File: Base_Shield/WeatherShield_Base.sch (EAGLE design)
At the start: 78 parts, among them Q1 BSS138, Q2 BSS138, U1 DS3231SN, U2 LT3652, U4 MPL3115A2LGA8, U5 HTU21D

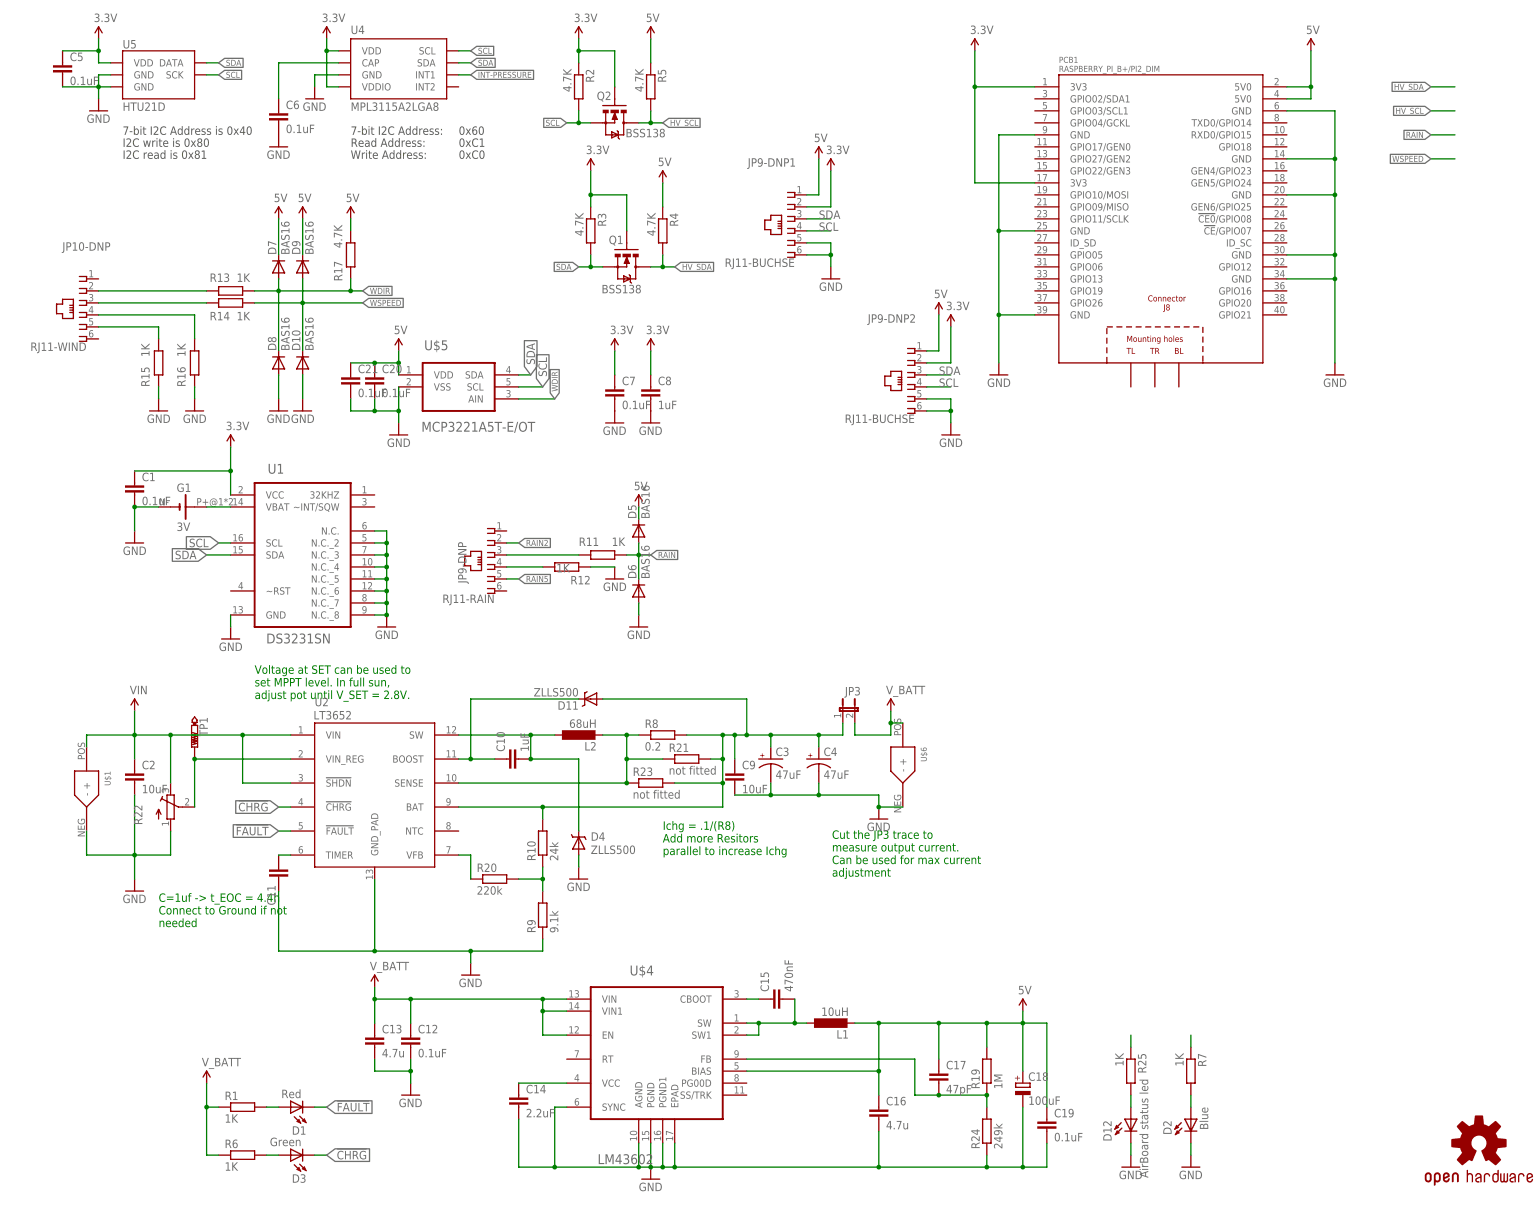
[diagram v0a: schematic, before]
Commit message: WeatherShield v1
Restructuration des Fichiers
Division en Air et Base Board
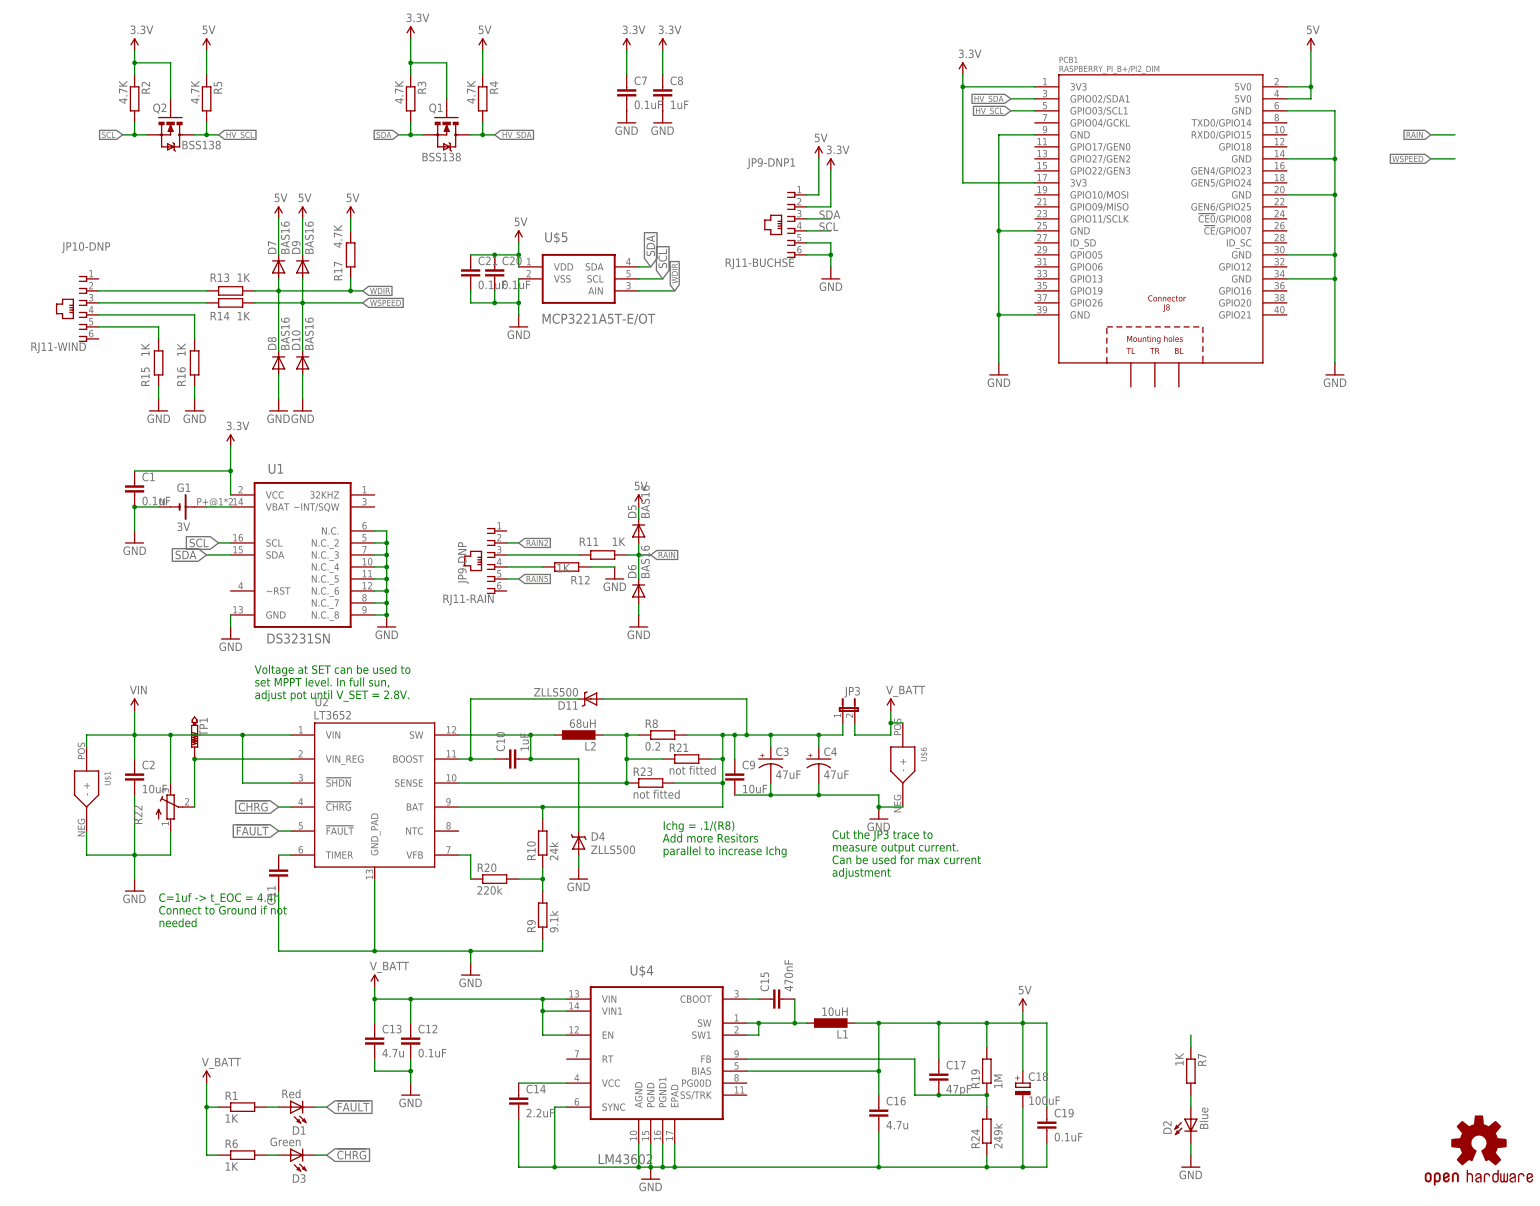
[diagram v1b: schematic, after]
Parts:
- removed C5, C6: 0.1uF, rcl:C-EUC0603
- removed D12: AirBoard status led, SparkFun:LED0603
- removed JP9-DNP2: RJ11-BUCHSE, FSEWeatherShield:RJ11-BUCHSE
- removed R25: 1K, rcl:R-EU_R0603
- removed U4: MPL3115A2LGA8, SparkFun-Sensors:MPL3115A2LGA8
- removed U5: HTU21D, SparkFun-Sensors:HTU21DSMD
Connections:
- removed net INT-PRESSURE: U4.INT1
- removed net N$28: D12.A, R25.2
- removed net N$5: C6.1, U4.CAP
- removed net STAT1: R25.1
- net 3.3V: no longer C5.1, JP9-DNP2.2, U4.VDD, U4.VDDIO, U5.VDD
- net 5V: no longer JP9-DNP2.1
- net GND: no longer C5.2, C6.2, D12.C, JP9-DNP2.5, JP9-DNP2.6, U4.GND, U5.GND@2, U5.GND@7
- net HV_SCL: now also PCB1.GPIO03/SCL1
- net HV_SDA: now also PCB1.GPIO02/SDA1
- net SCL: no longer JP9-DNP2.4, U4.SCL, U5.SCK
- net SDA: no longer JP9-DNP2.3, U4.SDA, U5.DATA
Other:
- note removed: "0x60"
- note removed: "0xC0"
- note removed: "0xC1"
- note removed: "7-bit I2C Address is 0x40"
- note removed: "7-bit I2C Address:"
- note removed: "Humidity"
- note removed: "I2C read is 0x81"
- note removed: "I2C write is 0x80"
- note removed: "Pressure"
- note removed: "Read Address:"
- note removed: "Write Address:"
- moved on the sheet: C20, C21, C7, C8, Q1, Q2, R2, R3, R4, R5, U$5

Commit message: WeatherShield_v1
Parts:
- removed U$5: MCP3221A5T-E/OT, FSEWeatherShield:MCP3221A5T-E/OT
- added C5: 0.1uF, rcl:C-EUC0603
- added JP1, JP2, JP4: (no value), pinhead:PINHD-1X2
- added JP5: (no value), pinhead:PINHD-1X3
- added JP6, JP7, JP8: (no value), pinhead:PINHD-1X1
- added U3: TMP100MDBVREP, FSEWeatherShield:TMP100MDBVREP
- added U4: ADS1015IDGST, FSEWeatherShield:ADS1015IDGST
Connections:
- new net N$14: JP6.1, U4.AIN1
- new net N$18: JP4.1, PCB1.TXD0/GPIO14
- new net N$19: JP4.2, PCB1.RXD0/GPIO15
- new net N$20: JP5.3, PCB1.GPIO10/MOSI
- new net N$21: JP5.2, PCB1.GPIO09/MISO
- new net N$25: JP5.1, PCB1.GPIO11/SCLK
- new net N$8: JP7.1, U4.AIN2
- new net N$9: JP8.1, U4.AIN3
- net 3.3V: now also C5.1, JP2.1, U3.V+
- net 5V: now also JP1.1, U4.VDD; no longer C20.1, C21.1, U$5.VDD
- net GND: now also C5.2, JP1.2, JP2.2, U3.AD0, U3.AD1, U3.GND, U4.ADDR, U4.GND; no longer C20.2, C21.2, U$5.VSS
- net HV_SCL: now also U4.SCL; no longer PCB1.GPIO03/SCL1
- net HV_SDA: now also U4.SDA; no longer PCB1.GPIO02/SDA1
- net RAIN: now also PCB1.GPIO18
- net SCL: now also PCB1.GPIO03/SCL1, U3.SCL; no longer U$5.SCL
- net SDA: now also PCB1.GPIO02/SDA1, U3.SDA; no longer U$5.SDA
- net STAT3: now also PCB1.GPIO21
- net WDIR: now also U4.AIN0; no longer U$5.AIN
- net WSPEED: now also PCB1.GPIO17/GEN0
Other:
- note added: "7-Bit I2C Address is 0x48"
- note added: "7-Bit I2C Address is 0x68"
- note added: "Add. SPI"
- note added: "Add. UART"
- note added: "Air Board Interface"
- note added: "Level shifter"
- note added: "Solar cell"
- note added: "Temperatur sensor"
- moved on the sheet: C1, C10, C11, C12, C13, C14, C15, C16, C17, C18, C19, C2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

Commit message: WeatherShield_v1
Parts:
- removed D10, D5, D6, D7, D8, D9: BAS16, SparkFun:DIODESOD
- removed R11, R13, R15, R16: 1K, rcl:R-EU_R0603
- R12, R14: value 1K -> 3k9
- R17: value 4.7K -> 10k
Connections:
- removed net N$1: JP10-DNP.3, R14.2
- removed net N$11: JP9-DNP.4, R12.1
- removed net N$12: JP10-DNP.5, R15.1
- removed net N$13: JP10-DNP.4, R16.1
- removed net N$2: JP10-DNP.2, R13.2
- removed net N$4: JP9-DNP.3, R11.2
- removed net RAIN2: JP9-DNP.2
- removed net RAIN5: JP9-DNP.5
- net 3.3V: now also JP10-DNP.3, JP9-DNP.3
- net 5V: no longer D5.C, D7.C, D9.C
- net GND: now also JP10-DNP.5, R14.2; no longer D10.A, D6.A, D8.A, R15.2, R16.2
- net RAIN: now also JP9-DNP.4, R12.1; no longer D5.A, D6.C, R11.1
- net WDIR: now also JP10-DNP.2; no longer D7.A, D8.C, R13.1
- net WSPEED: now also JP10-DNP.4; no longer D10.C, D9.A
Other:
- note added: "ADC 2 I2C"
- moved on the sheet: JP6, JP7, JP8, JP9-DNP, R12, R14, R17, U4

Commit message: WeatherShield_v1
routing....
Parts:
- added C6: 0.1uF, rcl:C-EUC0603
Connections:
- net 5V: now also C6.1
- net GND: now also C6.2
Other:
- moved on the sheet: C21
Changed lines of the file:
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@@
 <part name="P+6" library="SparkFun" deviceset="3.3V" device=""/>
 <part name="P+8" library="SparkFun" deviceset="3.3V" device=""/>
+<part name="C6" library="rcl" deviceset="C-EU" device="C0603" value="0.1uF"/>
 </parts>
 <sheets>
@@
 <instance part="GND23" gate="1" x="363.22" y="111.76" rot="MR0"/>
 <instance part="C20" gate="G$1" x="213.36" y="203.2"/>
-<instance part="C21" gate="G$1" x="208.28" y="203.2"/>
+<instance part="C21" gate="G$1" x="223.52" y="205.74"/>
 <instance part="R22" gate="1" x="40.64" y="48.26"/>
 <instance part="JP9-DNP1" gate="G$1" x="165.1" y="238.76" smashed="yes" rot="MR0">
@@
 <instance part="C5" gate="G$1" x="147.32" y="121.92"/>
 <instance part="GND18" gate="1" x="91.44" y="162.56" rot="MR0"/>
-<instance part="SUPPLY14" gate="G$1" x="73.66" y="203.2"/>
+<instance part="SUPPLY14" gate="G$1" x="73.66" y="210.82"/>
 <instance part="U4" gate="A" x="96.52" y="185.42"/>
 <instance part="JP6" gate="G$1" x="68.58" y="175.26" rot="R180"/>
@@
 <instance part="GND3" gate="1" x="172.72" y="172.72" rot="MR0"/>
 <instance part="P+6" gate="G$1" x="172.72" y="203.2"/>
-<instance part="P+8" gate="G$1" x="22.86" y="187.96"/>
+<instance part="P+8" gate="G$1" x="22.86" y="203.2"/>
+<instance part="C6" gate="G$1" x="66.04" y="203.2"/>
 </instances>
 <busses>
@@
 <pinref part="U4" gate="A" pin="ADDR"/>
 <wire x1="91.44" y1="167.64" x2="91.44" y2="170.18" width="0.1524" layer="91"/>
-<wire x1="76.2" y1="190.5" x2="60.96" y2="190.5" width="0.1524" layer="91"/>
+<wire x1="76.2" y1="190.5" x2="66.04" y2="190.5" width="0.1524" layer="91"/>
+<wire x1="66.04" y1="190.5" x2="60.96" y2="190.5" width="0.1524" layer="91"/>
 <wire x1="60.96" y1="190.5" x2="60.96" y2="167.64" width="0.1524" layer="91"/>
 <wire x1="60.96" y1="167.64" x2="91.44" y2="167.64" width="0.1524" layer="91"/>
 <junction x="91.44" y="167.64"/>
+<pinref part="C6" gate="G$1" pin="2"/>
+<wire x1="66.04" y1="198.12" x2="66.04" y2="190.5" width="0.1524" layer="91"/>
+<junction x="66.04" y="190.5"/>
 </segment>
 <segment>
@@
 <pinref part="P+8" gate="G$1" pin="3.3V"/>
 <wire x1="15.24" y1="182.88" x2="22.86" y2="182.88" width="0.1524" layer="91"/>
-<wire x1="22.86" y1="182.88" x2="22.86" y2="187.96" width="0.1524" layer="91"/>
+<wire x1="22.86" y1="182.88" x2="22.86" y2="203.2" width="0.1524" layer="91"/>
 </segment>
 </net>
@@
 <segment>
 <wire x1="76.2" y1="195.58" x2="73.66" y2="195.58" width="0.1524" layer="91" style="longdash"/>
-<wire x1="73.66" y1="195.58" x2="73.66" y2="203.2" width="0.1524" layer="91" style="longdash"/>
+<wire x1="73.66" y1="195.58" x2="73.66" y2="208.28" width="0.1524" layer="91"/>
 <pinref part="SUPPLY14" gate="G$1" pin="5V"/>
 <pinref part="U4" gate="A" pin="VDD"/>
-</segment>
-</net>
+<pinref part="C6" gate="G$1" pin="1"/>
+<wire x1="73.66" y1="208.28" x2="73.66" y2="210.82" width="0.1524" layer="91"/>
+<wire x1="66.04" y1="205.74" x2="66.04" y2="208.28" width="0.1524" layer="91"/>
+<wire x1="66.04" y1="208.28" x2="73.66" y2="208.28" width="0.1524" layer="91"/>
+<junction x="73.66" y="208.28"/>
+</segment>
+</net>

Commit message: WeatherShield_v1
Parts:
- removed C20, C21: 0.1uF, rcl:C-EUC0603
- removed LOGO1: OSHW-LOGOM, SparkFun-Aesthetics:OSHW-LOGOM
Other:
- note added: "+5V Generation (Raspberry Power)"
- moved on the sheet: C1, C10, C11, C12, C13, C14, C15, C16, C17, C18, C19, C2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

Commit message: WeatherShield_v1
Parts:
- renumbered U$1 to SOLAR_CELL, U$6 to BATT
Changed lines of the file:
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@@
 <part name="SUPPLY12" library="SparkFun-Aesthetics" deviceset="5V" device=""/>
 <part name="P+1" library="SparkFun" deviceset="VCC" device="" value="3.3V"/>
-<part name="U$1" library="FSEWeatherShield" deviceset="XT-60" device=""/>
-<part name="U$6" library="FSEWeatherShield" deviceset="XT-60" device=""/>
+<part name="SOLAR_CELL" library="FSEWeatherShield" deviceset="XT-60" device=""/>
+<part name="BATT" library="FSEWeatherShield" deviceset="XT-60" device=""/>
 <part name="JP1" library="pinhead" deviceset="PINHD-1X2" device=""/>
 <part name="JP2" library="pinhead" deviceset="PINHD-1X2" device=""/>
@@
 <text x="172.72" y="71.12" size="1.778" layer="95">Add. SPI</text>
 <text x="159.258" y="8.382" size="2.54" layer="98" rot="R90">Level shifter</text>
-<text x="129.794" y="135.636" size="1.27" layer="98" rot="R180">Air Board Interface</text>
+<text x="132.334" y="133.096" size="1.27" layer="98" rot="R180">Air Board Interface</text>
 <text x="68.326" y="174.244" size="1.27" layer="98">Solar cell</text>
 <text x="2.54" y="106.68" size="1.27" layer="98">Temperatur sensor</text>
@@
 <instance part="C12" gate="G$1" x="10.16" y="33.02"/>
 <instance part="C19" gate="G$1" x="111.76" y="15.24"/>
-<instance part="SUPPLY13" gate="G$1" x="254" y="106.68"/>
+<instance part="SUPPLY13" gate="G$1" x="248.92" y="114.3"/>
 <instance part="GND22" gate="1" x="182.88" y="45.72" rot="MR0"/>
 <instance part="GND23" gate="1" x="259.08" y="66.04" rot="MR270"/>
@@
 <instance part="SUPPLY16" gate="G$1" x="134.62" y="134.62"/>
 <instance part="P+5" gate="G$1" x="137.16" y="132.08"/>
-<instance part="P+7" gate="G$1" x="175.26" y="109.22"/>
+<instance part="P+7" gate="G$1" x="175.26" y="114.3"/>
 <instance part="SUPPLY12" gate="G$1" x="104.14" y="38.1"/>
 <instance part="P+1" gate="1" x="129.54" y="99.06"/>
-<instance part="U$1" gate="G$1" x="7.62" y="157.48" rot="R270"/>
-<instance part="U$6" gate="G$1" x="180.34" y="162.56" rot="R270"/>
+<instance part="SOLAR_CELL" gate="G$1" x="7.62" y="157.48" rot="R270"/>
+<instance part="BATT" gate="G$1" x="180.34" y="162.56" rot="R270"/>
 <instance part="JP1" gate="G$1" x="259.08" y="144.78"/>
 <instance part="JP2" gate="G$1" x="259.08" y="134.62"/>
@@
 <wire x1="25.4" y1="142.24" x2="17.78" y2="142.24" width="0.1524" layer="91"/>
 <junction x="17.78" y="142.24"/>
-<pinref part="U$1" gate="G$1" pin="-"/>
+<pinref part="SOLAR_CELL" gate="G$1" pin="-"/>
 <wire x1="7.62" y1="147.32" x2="7.62" y2="142.24" width="0.1524" layer="91"/>
 <wire x1="7.62" y1="142.24" x2="17.78" y2="142.24" width="0.1524" layer="91"/>
@@
 <pinref part="GND13" gate="1" pin="GND"/>
 <wire x1="175.26" y1="152.4" x2="175.26" y2="154.94" width="0.1524" layer="91"/>
-<pinref part="U$6" gate="G$1" pin="-"/>
+<pinref part="BATT" gate="G$1" pin="-"/>
 <wire x1="180.34" y1="152.4" x2="175.26" y2="152.4" width="0.1524" layer="91"/>
 <junction x="175.26" y="152.4"/>
@@
 <pinref part="PCB1" gate="G$1" pin="3V3@1"/>
 <wire x1="190.5" y1="106.68" x2="175.26" y2="106.68" width="0.1524" layer="91"/>
-<wire x1="175.26" y1="106.68" x2="175.26" y2="109.22" width="0.1524" layer="91"/>
+<wire x1="175.26" y1="106.68" x2="175.26" y2="114.3" width="0.1524" layer="91"/>
 <pinref part="PCB1" gate="G$1" pin="3V3@2"/>
 <wire x1="190.5" y1="86.36" x2="175.26" y2="86.36" width="0.1524" layer="91"/>
@@
 <pinref part="PCB1" gate="G$1" pin="5V0@1"/>
 <wire x1="248.92" y1="106.68" x2="243.84" y2="106.68" width="0.1524" layer="91"/>
-<wire x1="248.92" y1="106.68" x2="254" y2="106.68" width="0.1524" layer="91"/>
+<wire x1="248.92" y1="106.68" x2="248.92" y2="114.3" width="0.1524" layer="91"/>
 <junction x="248.92" y="106.68"/>
 <pinref part="SUPPLY13" gate="G$1" pin="5V"/>
@@
 <junction x="25.4" y="167.64"/>
 <pinref part="R22" gate="1" pin="E"/>
-<pinref part="U$1" gate="G$1" pin="+"/>
+<pinref part="SOLAR_CELL" gate="G$1" pin="+"/>
 <wire x1="7.62" y1="165.1" x2="7.62" y2="167.64" width="0.1524" layer="91"/>
 <wire x1="7.62" y1="167.64" x2="17.78" y2="167.64" width="0.1524" layer="91"/>
@@
 <wire x1="170.18" y1="170.18" x2="170.18" y2="167.64" width="0.1524" layer="91"/>
 <wire x1="170.18" y1="167.64" x2="177.8" y2="167.64" width="0.1524" layer="91"/>
-<pinref part="U$6" gate="G$1" pin="+"/>
+<pinref part="BATT" gate="G$1" pin="+"/>
 <wire x1="180.34" y1="170.18" x2="177.8" y2="170.18" width="0.1524" layer="91"/>
 <junction x="177.8" y="170.18"/>

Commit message: WeatherShield_v1
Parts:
- removed G1: 3V, battery:BATTERY-HOLDER_11.6MM
- removed JP6: (no value), pinhead:PINHD-1X1
- added JP10, JP11, JP12, JP9: (no value), pinhead:PINHD-1X1
- added R11, R13: 0, rcl:R-EU_R0603
- added TP2: SET, testpad:PTR1B1,27
- added U$1: BATTERIE_HALTER_CR1225, FSEWeatherShield:BATTERIE_HALTER_CR1225
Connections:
- removed net N$14: JP6.1, U4.AIN1
- removed net N$6: G1.+, U1.VBAT
- new net FAULT_PIN: D1.A, PCB1.GPIO04/GCKL, R1.2
- new net N$1: R13.1, R9.2
- new net N$2: R10.2, R11.1
- new net RTC_BATT: U$1.+, U1.VBAT, U4.AIN1
- net FB: now also R13.2; no longer R9.2
- net GND: now also U$1.-; no longer G1.-
- net HV_SCL: now also JP9.1
- net HV_SDA: now also JP12.1
- net N$16: now also R11.2; no longer R10.2
- net N$3: now also PCB1.GEN4/GPIO23; no longer D1.A, R1.2
- net SCL: now also JP11.1
- net SDA: now also JP10.1
- net V_BATT: now also TP2.TP
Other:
- moved on the sheet: C1, R9

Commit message: WeatherShield_v1
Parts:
- U$1: value BATTERIE_HALTER_CR1225 -> CR1225
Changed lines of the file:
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@@
 <part name="JP10" library="pinhead" deviceset="PINHD-1X1" device=""/>
 <part name="JP12" library="pinhead" deviceset="PINHD-1X1" device=""/>
-<part name="U$1" library="FSEWeatherShield" deviceset="BATTERIE_HALTER_CR1225" device=""/>
+<part name="U$1" library="FSEWeatherShield" deviceset="BATTERIE_HALTER_CR1225" device="" value="CR1225"/>
 </parts>
 <sheets>
@@
 <pinref part="U1" gate="A" pin="VBAT"/>
 <wire x1="127" y1="88.9" x2="129.54" y2="88.9" width="0.1524" layer="91"/>
-<wire x1="127" y1="88.9" x2="127" y2="86.36" width="0.1524" layer="91"/>
-<label x="127" y="86.36" size="1.778" layer="95" xref="yes"/>
+<wire x1="127" y1="88.9" x2="127" y2="101.6" width="0.1524" layer="91"/>
+<label x="127" y="101.6" size="1.778" layer="95" rot="R180" xref="yes"/>
 <pinref part="U$1" gate="G$1" pin="+"/>
 <junction x="127" y="88.9"/>
